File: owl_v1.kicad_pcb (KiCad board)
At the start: 2 copper layers, 63 parts, among them J1 USB_C_Receptacle_USB2.0_16P, J10 JST-PH Battery, J2 SWD, J3 Screw_Terminal_01x03, J4 SPI1_IMU, J5 I2C, J6 Micro_SD_Card_Det_Hirose_DM3AT, J7 I2C OLED, J8 External GPIOs, SW1 SW_SPDT, U1 STM32F103C8T6, U3 FT230XS, U4 SN65HVD230, U5 TLV73333PDBV, Y1 8MHz, Y2 32k768

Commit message: [checkpoint] Change from 2 layer to 4 layer PCB
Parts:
- moved SW1 157.7 mm to (275.3, 97.9)
- moved J7 97.8 mm to (188.7, 93.5)
- moved D1 86.6 mm to (179.2, 93.8)
- moved D2 86.6 mm to (179.2, 97.8)
- moved D3 86.6 mm to (179.2, 102.3)
- moved R10 86.6 mm to (183.2, 93.8)
- moved R17 86.6 mm to (183.2, 97.8)
- moved R18 86.6 mm to (183.2, 102.3)
- moved J4 79.8 mm to (188.8, 105.6), turned to 0 degrees
- moved TP3 68.9 mm to (173.4, 93.1)
- moved C11 67.8 mm to (183.5, 107.0)
- moved C12 67.8 mm to (183.5, 109.6)
- moved C13 67.8 mm to (183.5, 112.1)
- moved R4 67.8 mm to (183.5, 114.6)
- moved R5 67.8 mm to (183.5, 116.8)
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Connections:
- J6 pad SH: unconnected-(J6-SHIELD-PadSH) -> GND
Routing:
- net +3.3V: track 28.6 -> 48.4 mm
- net GND: track 59.3 -> 78.7 mm, vias 20 -> 21
- net CAN_TX: track 6.97 -> 20.8 mm
- net Net-(J6-DET_A): track 0.00 -> 13.6 mm
- net CAN_RX: track 7.13 -> 18.6 mm
- net Net-(U1-BOOT0): track 5.96 -> 0.00 mm
- net I2C_SDA: track 5.62 -> 0.00 mm
- net I2C_SCLK: track 5.35 -> 0.00 mm
- net LED_GREEN: track 5.22 -> 0.00 mm
- net LED_BLUE: track 4.94 -> 0.00 mm
- net TRACE_SWO: track 4.39 -> 0.00 mm
- net GPIO_7: track 4.38 -> 0.00 mm
- net SWCLK: track 3.97 -> 0.00 mm
- net SD_MISO: track 0.00 -> 3.26 mm
- net Net-(J6-DAT1): track 0.00 -> 2.38 mm
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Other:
- board outline added: 39.7 x 83.3 mm
- copper layers 2 -> 4

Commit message: [feat] Routing for FT230X USB-UART
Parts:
- moved SW1 98.5 mm to (180.5, 124.8)
- moved D1 36.5 mm to (160.8, 125.4), turned to -90 degrees
- moved R10 35.5 mm to (160.8, 121.4), turned to 90 degrees
- moved D2 34.9 mm to (157.8, 125.4), turned to -90 degrees
- moved R17 34.6 mm to (157.8, 121.3), turned to 90 degrees
- moved R18 34.2 mm to (154.8, 121.4), turned to 90 degrees
- moved D3 33.6 mm to (154.8, 125.4), turned to -90 degrees
- moved R2 25.7 mm to (181.5, 117.1)
- moved U3 21.3 mm to (175.5, 109.9), turned to 0 degrees
- moved TP1 19.5 mm to (170.3, 117.1)
- moved TP3 16.8 mm to (159.9, 103.1)
- moved R5 10.7 mm to (173.0, 114.5), turned to 90 degrees
- moved C11 10.3 mm to (176.4, 114.5), turned to 90 degrees
- moved C12 10.1 mm to (174.7, 114.5), turned to 90 degrees
- moved R4 5.26 mm to (178.2, 114.5), turned to 90 degrees
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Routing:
- net +3.3V: track 48.4 -> 25.3 mm, vias 0 -> 3
- net GND: track 78.7 -> 56.2 mm, vias 21 -> 22
- net CAN_TX: track 20.8 -> 0.00 mm
- net CAN_RX: track 18.6 -> 0.00 mm
- net /owl_v1/Power Regulation/USB_OUT_D-: track 0.00 -> 17.3 mm, vias 0 -> 2
- net /owl_v1/Power Regulation/USB_OUT_D+: track 0.00 -> 11.7 mm
- net Net-(J1-CC2): track 2.20 -> 11.5 mm, vias 0 -> 2
- net Net-(J1-CC1): track 0.00 -> 7.68 mm, vias 0 -> 2
- net Net-(U3-USBDP): track 0.00 -> 1.63 mm
- net Net-(U3-USBDM): track 0.00 -> 1.61 mm
- net VBUS: track 24.0 -> 22.7 mm
- net +5V: track 11.6 -> 12.7 mm, vias 0 -> 2
- added copper zone on In2.Cu, net +3.3V
- added copper zone on In1.Cu, net GND

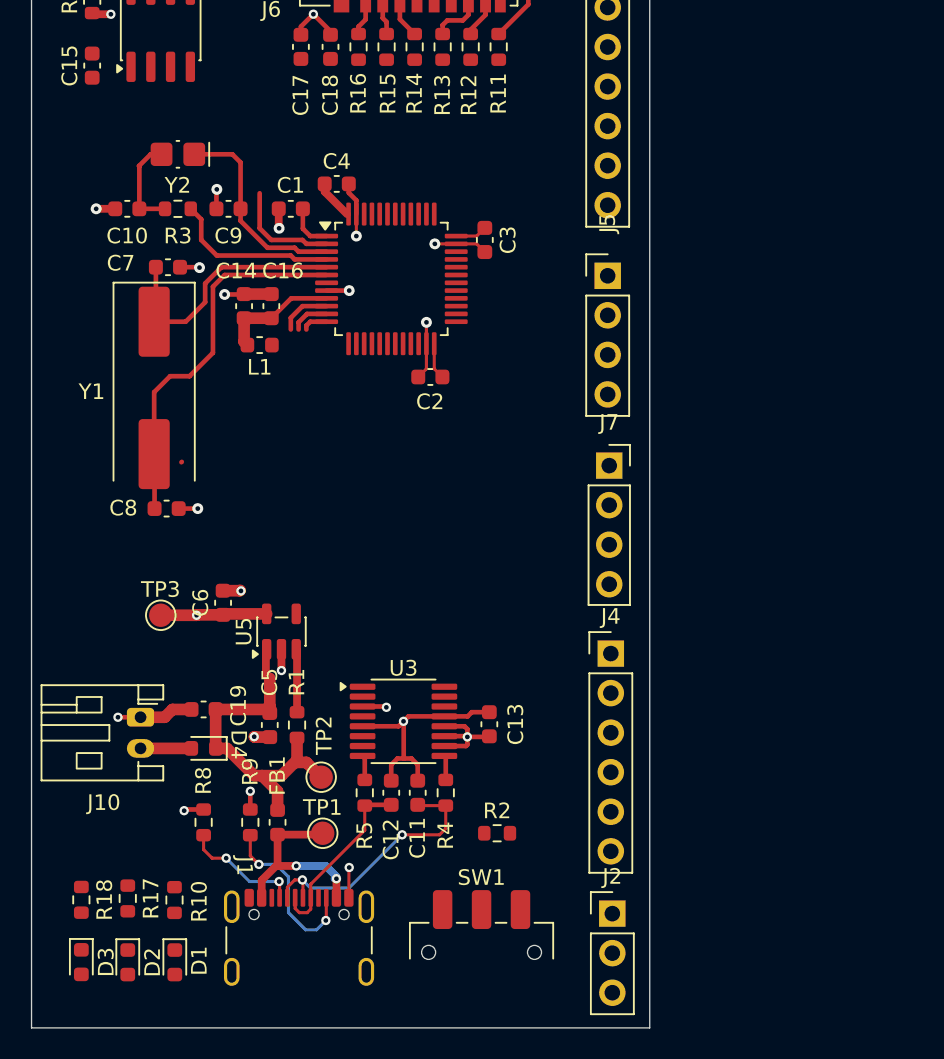
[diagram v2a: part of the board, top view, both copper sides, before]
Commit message: [feat] Finished re-routing HSE, LSE and 3.3VA
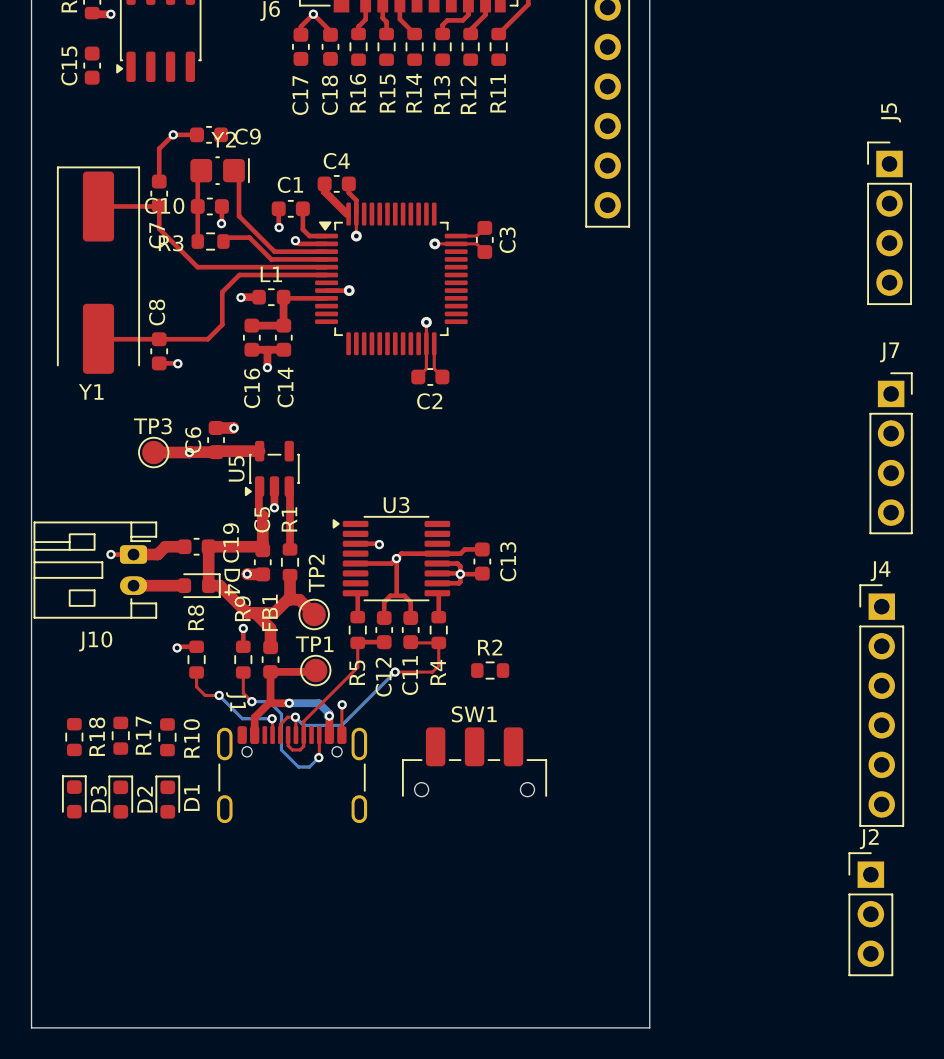
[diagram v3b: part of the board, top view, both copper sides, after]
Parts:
- moved J5 19.5 mm to (206.7, 74.1)
- moved J7 18.7 mm to (206.8, 88.9)
- moved J4 17.7 mm to (206.2, 102.5)
- moved J2 16.8 mm to (205.5, 119.8)
- moved C11 10.5 mm to (175.9, 104.0)
- moved C19 10.5 mm to (162.2, 98.7)
- moved C5 10.5 mm to (166.4, 99.7)
- moved C6 10.5 mm to (163.4, 91.8)
- moved D1 10.5 mm to (160.3, 114.9)
- moved D3 10.5 mm to (154.3, 114.9)
- moved D4 10.5 mm to (162.2, 101.2)
- moved FB1 10.5 mm to (166.9, 106.0)
- moved R1 10.5 mm to (168.2, 99.7)
- moved R18 10.5 mm to (154.3, 110.9)
- moved R8 10.5 mm to (162.2, 106.0)
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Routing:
- net HSE_OSC_OUT: track 24.5 -> 17.6 mm
- net GPIO_8: track 6.96 -> 2.08 mm, vias 0 -> 1
- net LSE_OSC_OUT: track 10.8 -> 6.88 mm
- net LSE_OSC_IN: track 13.3 -> 9.49 mm
- net GPIO_0: track 3.36 -> 0.00 mm
- net GPIO_1: track 2.48 -> 0.00 mm
- net GND: track 56.2 -> 58.6 mm, vias 22 -> 21
- net Net-(C10-Pad1): track 6.17 -> 4.39 mm
- net GPIO_2: track 1.65 -> 0.00 mm
- net +3.3V: track 25.3 -> 26.5 mm, vias 3 -> 4
- net +3.3VA: track 7.64 -> 7.03 mm

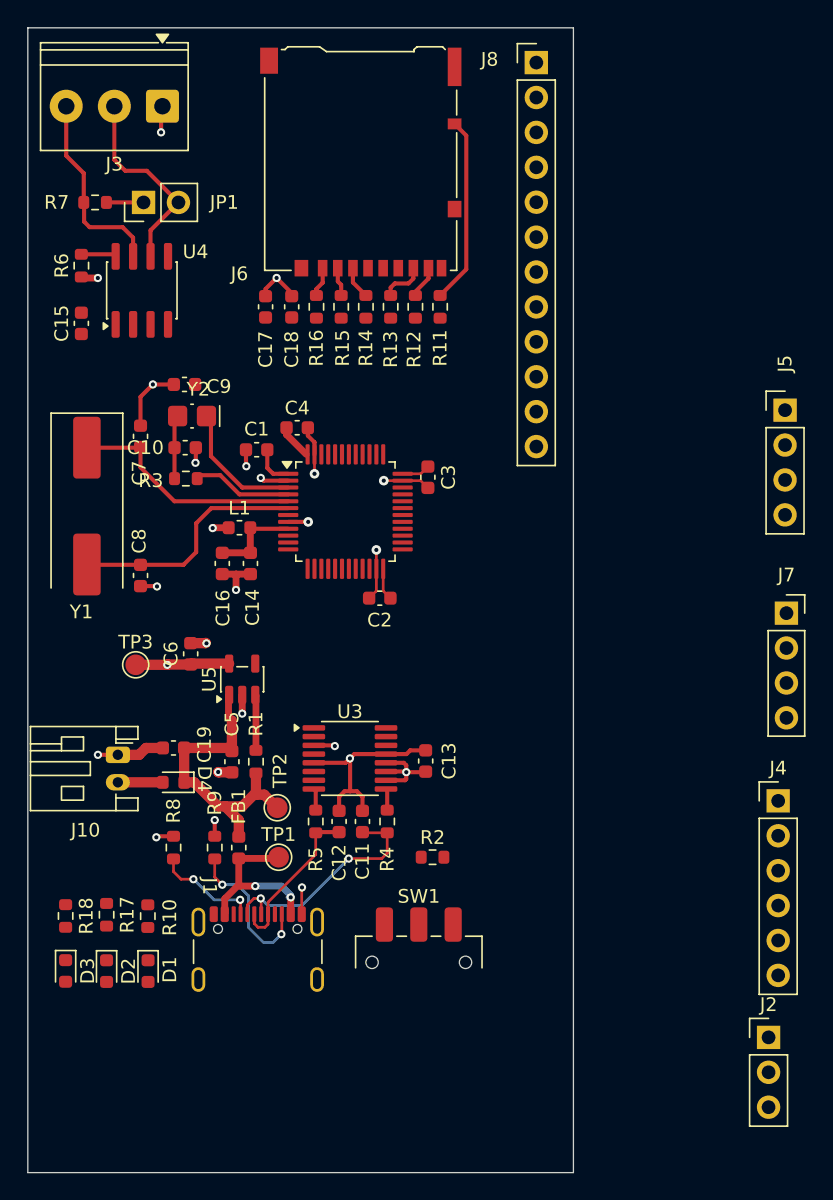
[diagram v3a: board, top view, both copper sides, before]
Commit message: [refactor] Board resizing, SWD moved to fit left side of the board
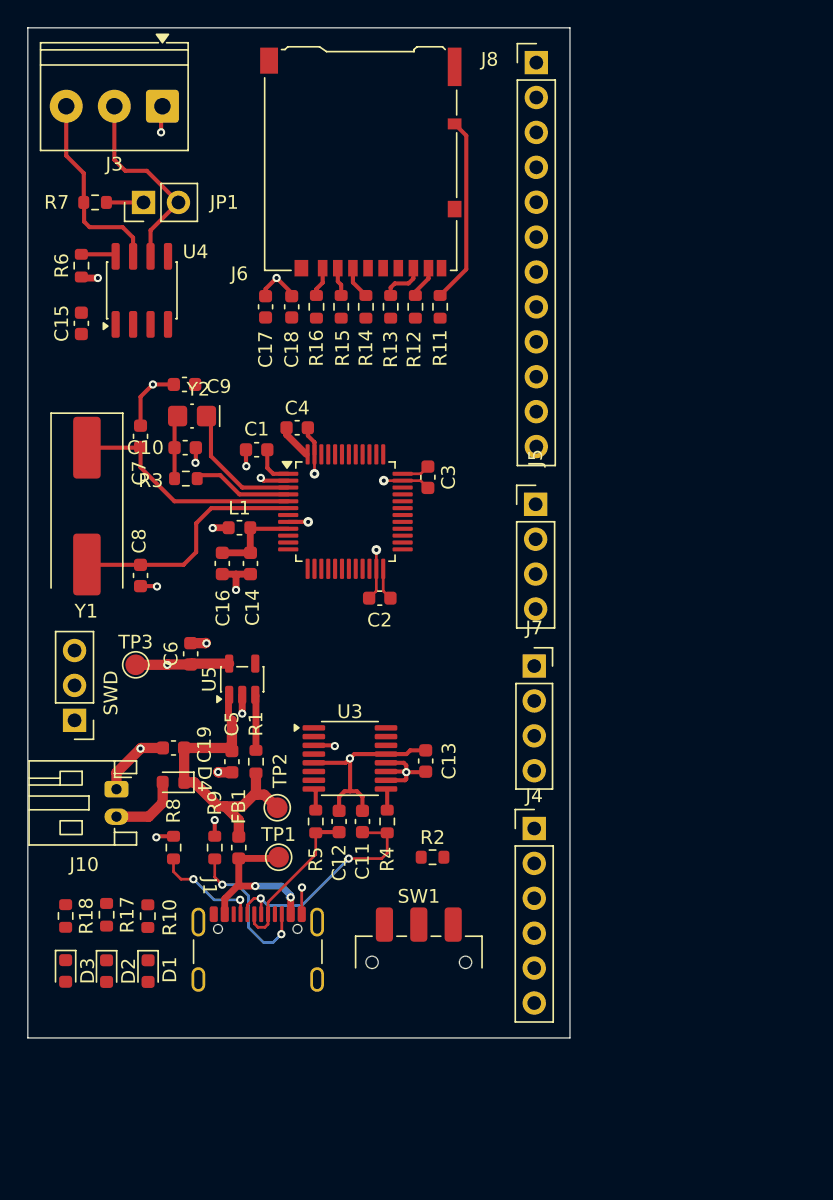
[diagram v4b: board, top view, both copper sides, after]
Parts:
- moved SWD 55.5 mm to (155.0, 96.7), turned to 180 degrees
- moved J5 19.4 mm to (188.6, 81.0)
- moved J7 18.7 mm to (188.4, 92.7)
- moved J4 17.9 mm to (188.4, 104.6)
- moved J10 2.50 mm to (158.1, 101.7)
- renumbered J2 to SWD
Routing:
- net VBAT: track 3.26 -> 5.27 mm
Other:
- board size 39.7 x 83.3 mm -> 39.5 x 73.5 mm
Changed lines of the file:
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@@
 	(footprint "Connector_JST:JST_PH_S2B-PH-K_1x02_P2.00mm_Horizontal"
 		(layer "F.Cu")
-		(at 158.15 99.2 -90)
+		(at 158.05 101.7 -90)
 		(descr "JST PH series connector, S2B-PH-K (http://www.jst-mfg.com/product/pdf/eng/ePH.pdf)")
 		(tags "connector JST PH horizontal")
@@
 	(footprint "Connector_PinSocket_2.54mm:PinSocket_1x04_P2.54mm_Vertical"
 		(layer "F.Cu")
-		(at 206.8 88.89)
+		(at 188.45 92.74)
 		(descr "Through hole straight socket strip, 1x04, 2.54mm pitch, single row (from Kicad 4.0.7), script generated")
 		(tags "Through hole socket strip THT 1x04 2.54mm single row")
@@
 	(footprint "Connector_PinHeader_2.54mm:PinHeader_1x04_P2.54mm_Vertical"
 		(layer "F.Cu")
-		(at 206.7 74.12)
+		(at 188.55 80.97)
 		(descr "Through hole straight pin header, 1x04, 2.54mm pitch, single row")
 		(tags "Through hole pin header THT 1x04 2.54mm single row")
@@
 	(footprint "Connector_PinHeader_2.54mm:PinHeader_1x06_P2.54mm_Vertical"
 		(layer "F.Cu")
-		(at 206.2 102.55)
+		(at 188.45 104.56)
 		(descr "Through hole straight pin header, 1x06, 2.54mm pitch, single row")
 		(tags "Through hole pin header THT 1x06 2.54mm single row")
@@
 	(footprint "Connector_PinHeader_2.54mm:PinHeader_1x03_P2.54mm_Vertical"
 		(layer "F.Cu")
-		(at 205.5 119.76)
+		(at 155 96.69 180)
 		(descr "Through hole straight pin header, 1x03, 2.54mm pitch, single row")
 		(tags "Through hole pin header THT 1x03 2.54mm single row")
-		(property "Reference" "J2"
-			(at 0 -2.38 0)
+		(property "Reference" "SWD"
+			(at -2.65 1.99 90)
 			(layer "F.SilkS")
 			(effects
@@
 		(duplicate_pad_numbers_are_jumpers no)
 		(fp_line
-			(start -1.38 -1.38)
-			(end 0 -1.38)
+			(start 1.38 1.27)
+			(end 1.38 6.46)
 			(stroke
 				(width 0.12)
@@
 		)
 		(fp_line
-			(start -1.38 0)
-			(end -1.38 -1.38)
+			(start -1.38 6.46)
+			(end 1.38 6.46)
 			(stroke
 				(width 0.12)
@@
 		(fp_line
 			(start -1.38 1.27)
-			(end -1.38 6.46)
+			(end 1.38 1.27)
 			(stroke
 				(width 0.12)
@@
 		(fp_line
 			(start -1.38 1.27)
-			(end 1.38 1.27)
+			(end -1.38 6.46)
 			(stroke
 				(width 0.12)
@@
 		)
 		(fp_line
-			(start -1.38 6.46)
-			(end 1.38 6.46)
+			(start -1.38 0)
+			(end -1.38 -1.38)
 			(stroke
 				(width 0.12)
@@
 		)
 		(fp_line
-			(start 1.38 1.27)
-			(end 1.38 6.46)
+			(start -1.38 -1.38)
+			(end 0 -1.38)
 			(stroke
 				(width 0.12)
@@
 		)
 		(fp_line
-			(start -1.27 -0.635)
-			(end -0.635 -1.27)
+			(start 1.27 6.35)
+			(end -1.27 6.35)
 			(stroke
 				(width 0.1)
@@
 		)
 		(fp_line
-			(start -1.27 6.35)
-			(end -1.27 -0.635)
+			(start 1.27 -1.27)
+			(end 1.27 6.35)
 			(stroke
 				(width 0.1)
@@
 		)
 		(fp_line
-			(start 1.27 -1.27)
-			(end 1.27 6.35)
+			(start -1.27 6.35)
+			(end -1.27 -0.635)
 			(stroke
 				(width 0.1)
@@
 		)
 		(fp_line
-			(start 1.27 6.35)
-			(end -1.27 6.35)
+			(start -1.27 -0.635)
+			(end -0.635 -1.27)
 			(stroke
 				(width 0.1)
@@
 		)
 		(pad "1" thru_hole rect
-			(at 0 0)
+			(at 0 0 180)
 			(size 1.7 1.7)
 			(drill 1)
@@
 		)
 		(pad "2" thru_hole circle
-			(at 0 2.54)
+			(at 0 2.54 180)
 			(size 1.7 1.7)
 			(drill 1)
@@
 		)
 		(pad "3" thru_hole circle
-			(at 0 5.08)
+			(at 0 5.08 180)
 			(size 1.7 1.7)
 			(drill 1)
@@
 		(descr "HC-49-SD, Crystal, 11.4x4.7mm package, SMD, http://cdn-reichelt.de/documents/datenblatt/B400/xxx-HC49-SMD.pdf")
 		(property "Reference" "Y1"
-			(at 7.7 0.4 180)
+			(at 7.65 0.05 0)
 			(layer "F.SilkS")
 			(effects
@@
 	(gr_rect
 		(start 151.6 46.3)
-		(end 191.3 129.6)
+		(end 191.05 119.8)
 		(stroke
 			(width 0.05)
@@
 	)
 	(segment
+		(start 159.85 98.7)
+		(end 159.8 98.75)
+		(width 0.75)
+		(layer "F.Cu")
+		(net "GND")
+	)
+	(segment
 		(start 163.825 76.85)
 		(end 163.825 77.925)
@@
 	)
 	(segment
-		(start 160.2 98.7)
-		(end 161.425 98.7)
-		(width 0.75)
-		(layer "F.Cu")
-		(net "GND")
-	)
-	(segment
 		(start 172.46 78.5)
 		(end 172.46 77.3375)
@@
 	)
 	(segment
-		(start 159.7 99.2)
-		(end 160.2 98.7)
-		(width 0.75)
-		(layer "F.Cu")
-		(net "GND")
-	)
-	(segment
 		(start 165.475 100.475)
 		(end 165.45 100.45)
@@
 	)
 	(segment
+		(start 158.05 100.5)
+		(end 159.8 98.75)
+		(width 0.75)
+		(layer "F.Cu")
+		(net "GND")
+	)
+	(segment
 		(start 176.96 84.29)
 		(end 176.96 85.6625)
@@
 	)
 	(segment
+		(start 158.05 101.7)
+		(end 158.05 100.5)
+		(width 0.75)
+		(layer "F.Cu")
+		(net "GND")
+	)
+	(segment
 		(start 179.425 98.875)
 		(end 180.55 98.875)
@@
 	)
 	(segment
+		(start 161.425 98.7)
+		(end 159.85 98.7)
+		(width 0.75)
+		(layer "F.Cu")
+		(net "GND")
+	)
+	(segment
 		(start 174.25 102.25)
 		(end 174.65 101.85)
@@
 	)
 	(segment
-		(start 158.15 99.2)
-		(end 159.7 99.2)
-		(width 0.75)
-		(layer "F.Cu")
-		(net "GND")
-	)
-	(segment
 		(start 175.0375 99.4625)
 		(end 175.355 99.145)
@@
 	)
 	(segment
-		(start 158.15 99.2)
-		(end 156.7 99.2)
-		(width 0.3)
-		(layer "F.Cu")
-		(net "GND")
-	)
-	(segment
 		(start 171.975 75.975)
 		(end 171.975 75.4)
@@
 	)
 	(via
-		(at 156.7 99.2)
+		(at 165.2 103.95)
 		(size 0.6)
 		(drill 0.3)
@@
 	)
 	(via
-		(at 165.2 103.95)
+		(at 156.695 64.505)
 		(size 0.6)
 		(drill 0.3)
@@
 	)
 	(via
-		(at 156.695 64.505)
-		(size 0.6)
+		(at 172.46 78.75)
+		(size 0.7)
 		(drill 0.3)
 		(layers "F.Cu" "B.Cu")
@@
 	)
 	(via
-		(at 172.46 78.75)
-		(size 0.7)
+		(at 159.8 98.75)
+		(size 0.6)
 		(drill 0.3)
 		(layers "F.Cu" "B.Cu")
@@
 	)
 	(segment
-		(start 158.15 101.2)
+		(start 161.4125 102.6875)
 		(end 161.4125 101.2)
 		(width 0.75)
 		(layer "F.Cu")
+		(net "VBAT")
+	)
+	(segment
+		(start 160.4 103.7)
+		(end 161.4125 102.6875)
+		(width 0.75)
+		(layer "F.Cu")
+		(net "VBAT")
+	)
+	(segment
+		(start 158.05 103.7)
+		(end 160.4 103.7)
+		(width 0.75)
+		(layer "F.Cu")

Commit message: [feat] Finished routing for uSD card reader
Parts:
- moved J5 8.67 mm to (191.4, 89.1), turned to 180 degrees
- moved J7 8.38 mm to (191.5, 100.5), turned to 180 degrees
- moved J4 2.99 mm to (191.4, 105.0)
- moved J8 2.99 mm to (191.6, 49.3)
- moved SW1 2.41 mm to (182.4, 114.5)
- moved R2 2.41 mm to (183.4, 106.8)
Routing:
- net SD_CS: track 2.09 -> 37.7 mm, vias 0 -> 2
- net SD_SCK: track 0.00 -> 30.6 mm, vias 0 -> 2
- net SD_MOSI: track 2.38 -> 31.2 mm, vias 0 -> 2
- net SD_MISO: track 3.26 -> 31.6 mm, vias 0 -> 2
- net CAN_TX: track 0.00 -> 22.4 mm
- net GND: track 59.0 -> 79.6 mm, vias 21 -> 26
- net CAN_RX: track 0.00 -> 19.0 mm
- net /owl_v1/USB to UART Bridge/FT230_TXD: track 0.00 -> 5.08 mm, vias 0 -> 1
- net GPIO_6: track 0.00 -> 4.74 mm, vias 0 -> 1
- net +3.3V: track 26.5 -> 31.0 mm, vias 4 -> 7
- net /owl_v1/USB to UART Bridge/FT230_RXD: track 0.00 -> 3.22 mm, vias 0 -> 1
- net GPIO_4: track 0.00 -> 1.52 mm, vias 0 -> 1
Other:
- board size 39.5 x 73.5 mm -> 43.3 x 73.2 mm
